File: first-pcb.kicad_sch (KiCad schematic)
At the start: 7 parts

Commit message: Schematic Complete
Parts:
- added K1: my_connector, Connector_PinHeader_2.54mm:PinHeader_1x02_P2.54mm_Vertical, symbol my_library:my_connector
- added unit 2 of U1
- added unit 3 of U1
- BT1: renamed from BT?; footprint (none) -> Battery:BatteryHolder_Eagle_12BH611-GR
- C1: renamed from C?; footprint (none) -> Capacitor_THT:C_Disc_D3.0mm_W2.0mm_P2.50mm
- P1: renamed from P?; footprint (none) -> Potentiometer_THT:Potentiometer_Alps_RK09K_Single_Vertical
- U1: renamed from U?; footprint (none) -> Package_DIP:DIP-8_W7.62mm
- gave numbers to parts that had none: 3
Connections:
- net GND: now also K1.2, U1.4 (V-)
- net at BT1.1 (+), Q1.1 (C), R1.1: now also U1.8 (V+)
- net at U1.1: now also Q1.2 (B)
- net at Q1.3 (E), U1.2 (-): now also K1.1
- no-connect marks 0 -> 3

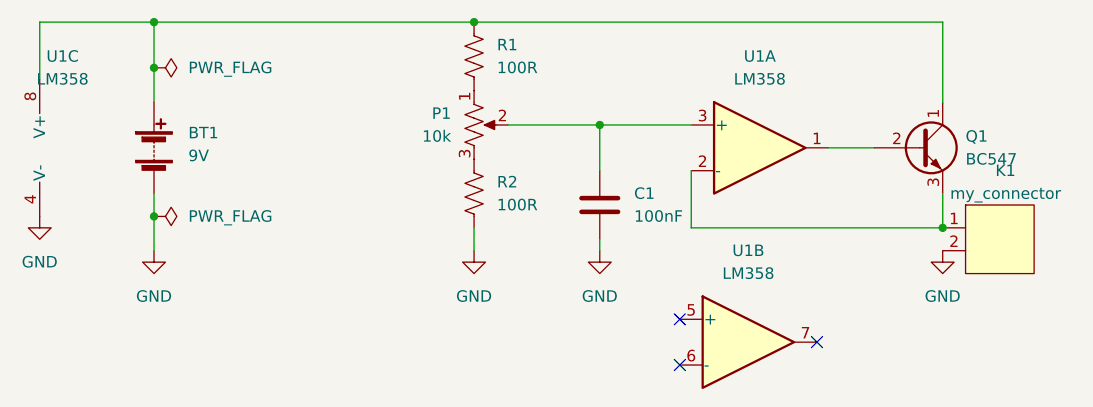
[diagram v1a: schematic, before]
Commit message: Add Grounding Pins/Mounting Holes
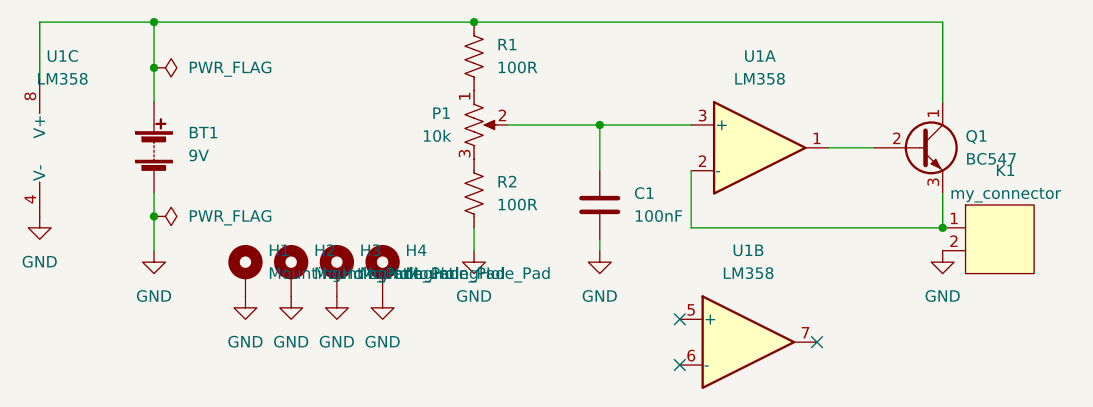
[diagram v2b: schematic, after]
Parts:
- added H1, H2, H3, H4: MountingHole_Pad, MountingHole:MountingHole_3.2mm_M3, symbol Mechanical:MountingHole_Pad
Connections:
- net GND: now also H1.1, H2.1, H3.1, H4.1
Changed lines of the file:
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@@
     (pin "2")
+  )
+  (symbol (lib_id "Mechanical:MountingHole_Pad") (at 67.31 106.68 0) (unit 1)
+    (in_bom yes) (on_board yes) (fields_autoplaced)
+    (property "Reference" "H4" (id 0) (at 69.85 104.1399 0)
+      (effects (font (size 1.27 1.27)) (justify left))
+    )
+    (property "Value" "MountingHole_Pad" (id 1) (at 69.85 106.6799 0)
+      (effects (font (size 1.27 1.27)) (justify left))
+    )
+    (property "Footprint" "MountingHole:MountingHole_3.2mm_M3" (id 2) (at 67.31 106.68 0)
+      (effects (font (size 1.27 1.27)) hide)
+    )
+    (property "Datasheet" "~" (id 3) (at 67.31 106.68 0)
+      (effects (font (size 1.27 1.27)) hide)
+    )
+    (pin "1")
+  )
+  (symbol (lib_id "power:GND") (at 52.07 109.22 0) (unit 1)
+    (in_bom yes) (on_board yes) (fields_autoplaced)
+    (property "Reference" "#PWR05" (id 0) (at 52.07 115.57 0)
+      (effects (font (size 1.27 1.27)) hide)
+    )
+    (property "Value" "GND" (id 1) (at 52.07 114.3 0))
+    (property "Footprint" "" (id 2) (at 52.07 109.22 0)
+      (effects (font (size 1.27 1.27)) hide)
+    )
+    (property "Datasheet" "" (id 3) (at 52.07 109.22 0)
+      (effects (font (size 1.27 1.27)) hide)
+    )
+    (pin "1")
   )
   (symbol (lib_id "Amplifier_Operational:LM358") (at 107.95 114.3 0) (unit 2)
@@
     (pin "1")
   )
+  (symbol (lib_id "power:GND") (at 57.15 109.22 0) (unit 1)
+    (in_bom yes) (on_board yes) (fields_autoplaced)
+    (property "Reference" "#PWR06" (id 0) (at 57.15 115.57 0)
+      (effects (font (size 1.27 1.27)) hide)
+    )
+    (property "Value" "GND" (id 1) (at 57.15 114.3 0))
+    (property "Footprint" "" (id 2) (at 57.15 109.22 0)
+      (effects (font (size 1.27 1.27)) hide)
+    )
+    (property "Datasheet" "" (id 3) (at 57.15 109.22 0)
+      (effects (font (size 1.27 1.27)) hide)
+    )
+    (pin "1")
+  )
+  (symbol (lib_id "Mechanical:MountingHole_Pad") (at 62.23 106.68 0) (unit 1)
+    (in_bom yes) (on_board yes) (fields_autoplaced)
+    (property "Reference" "H3" (id 0) (at 64.77 104.1399 0)
+      (effects (font (size 1.27 1.27)) (justify left))
+    )
+    (property "Value" "MountingHole_Pad" (id 1) (at 64.77 106.6799 0)
+      (effects (font (size 1.27 1.27)) (justify left))
+    )
+    (property "Footprint" "MountingHole:MountingHole_3.2mm_M3" (id 2) (at 62.23 106.68 0)
+      (effects (font (size 1.27 1.27)) hide)
+    )
+    (property "Datasheet" "~" (id 3) (at 62.23 106.68 0)
+      (effects (font (size 1.27 1.27)) hide)
+    )
+    (pin "1")
+  )
+  (symbol (lib_id "power:GND") (at 67.31 109.22 0) (unit 1)
+    (in_bom yes) (on_board yes) (fields_autoplaced)
+    (property "Reference" "#PWR08" (id 0) (at 67.31 115.57 0)
+      (effects (font (size 1.27 1.27)) hide)
+    )
+    (property "Value" "GND" (id 1) (at 67.31 114.3 0))
+    (property "Footprint" "" (id 2) (at 67.31 109.22 0)
+      (effects (font (size 1.27 1.27)) hide)
+    )
+    (property "Datasheet" "" (id 3) (at 67.31 109.22 0)
+      (effects (font (size 1.27 1.27)) hide)
+    )
+    (pin "1")
+  )
   (symbol (lib_id "power:GND") (at 129.54 104.14 0) (unit 1)
     (in_bom yes) (on_board yes) (fields_autoplaced)
@@
     (pin "1")
   )
+  (symbol (lib_id "power:GND") (at 62.23 109.22 0) (unit 1)
+    (in_bom yes) (on_board yes) (fields_autoplaced)
+    (property "Reference" "#PWR07" (id 0) (at 62.23 115.57 0)
+      (effects (font (size 1.27 1.27)) hide)
+    )
+    (property "Value" "GND" (id 1) (at 62.23 114.3 0))
+    (property "Footprint" "" (id 2) (at 62.23 109.22 0)
+      (effects (font (size 1.27 1.27)) hide)
+    )
+    (property "Datasheet" "" (id 3) (at 62.23 109.22 0)
+      (effects (font (size 1.27 1.27)) hide)
+    )
+    (pin "1")
+  )
   (symbol (lib_id "Device:R_US") (at 77.47 82.55 0) (unit 1)
     (in_bom yes) (on_board yes) (fields_autoplaced)
@@
     )
     (property "Datasheet" "~" (id 3) (at 41.91 100.33 0)
+      (effects (font (size 1.27 1.27)) hide)
+    )
+    (pin "1")
+  )
+  (symbol (lib_id "Mechanical:MountingHole_Pad") (at 57.15 106.68 0) (unit 1)
+    (in_bom yes) (on_board yes) (fields_autoplaced)
+    (property "Reference" "H2" (id 0) (at 59.69 104.1399 0)
+      (effects (font (size 1.27 1.27)) (justify left))
+    )
+    (property "Value" "MountingHole_Pad" (id 1) (at 59.69 106.6799 0)
+      (effects (font (size 1.27 1.27)) (justify left))
+    )
+    (property "Footprint" "MountingHole:MountingHole_3.2mm_M3" (id 2) (at 57.15 106.68 0)
+      (effects (font (size 1.27 1.27)) hide)
+    )
+    (property "Datasheet" "~" (id 3) (at 57.15 106.68 0)
       (effects (font (size 1.27 1.27)) hide)
     )
@@
     (pin "8")
   )
+  (symbol (lib_id "Mechanical:MountingHole_Pad") (at 52.07 106.68 0) (unit 1)
+    (in_bom yes) (on_board yes) (fields_autoplaced)
+    (property "Reference" "H1" (id 0) (at 54.61 104.1399 0)
+      (effects (font (size 1.27 1.27)) (justify left))
+    )
+    (property "Value" "MountingHole_Pad" (id 1) (at 54.61 106.6799 0)
+      (effects (font (size 1.27 1.27)) (justify left))
+    )
+    (property "Footprint" "MountingHole:MountingHole_3.2mm_M3" (id 2) (at 52.07 106.68 0)
+      (effects (font (size 1.27 1.27)) hide)
+    )
+    (property "Datasheet" "~" (id 3) (at 52.07 106.68 0)
+      (effects (font (size 1.27 1.27)) hide)
+    )
+    (pin "1")
+  )
   (symbol (lib_id "Device:R_US") (at 77.47 97.79 0) (unit 1)
     (in_bom yes) (on_board yes) (fields_autoplaced)
@@
       (reference "#PWR04") (unit 1) (value "GND") (footprint "")
     )
+    (path "/29a4dbbb-76df-4a5f-97bc-20e25b6c120d"
+      (reference "#PWR05") (unit 1) (value "GND") (footprint "")
+    )
+    (path "/6c5ddf50-598b-4624-97bc-707751a7cca0"
+      (reference "#PWR06") (unit 1) (value "GND") (footprint "")
+    )
+    (path "/ae2ab66b-9b4c-4dfe-8858-9502fff38c7b"
+      (reference "#PWR07") (unit 1) (value "GND") (footprint "")
+    )
+    (path "/939ef534-f1b7-45ad-a510-ae95db7deb2d"
+      (reference "#PWR08") (unit 1) (value "GND") (footprint "")
+    )
     (path "/64ebe1aa-d6a0-44a4-ab37-9850a83d8c0a"
       (reference "#PWR0101") (unit 1) (value "GND") (footprint "")
@@
       (reference "C1") (unit 1) (value "100nF") (footprint "Capacitor_THT:C_Disc_D3.0mm_W2.0mm_P2.50mm")
     )
+    (path "/e0ef2c2b-7a91-4865-8b62-e21cbba98aaa"
+      (reference "H1") (unit 1) (value "MountingHole_Pad") (footprint "MountingHole:MountingHole_3.2mm_M3")
+    )
+    (path "/d0603c93-1e0d-4f9c-9ae4-7cbc129674aa"
+      (reference "H2") (unit 1) (value "MountingHole_Pad") (footprint "MountingHole:MountingHole_3.2mm_M3")
+    )
+    (path "/85f2e531-45c2-4e3d-a8cf-17b5a7905d98"
+      (reference "H3") (unit 1) (value "MountingHole_Pad") (footprint "MountingHole:MountingHole_3.2mm_M3")
+    )
+    (path "/229409d0-9935-4be1-a852-23c013d0a939"
+      (reference "H4") (unit 1) (value "MountingHole_Pad") (footprint "MountingHole:MountingHole_3.2mm_M3")
+    )
     (path "/f45d5ac8-c98a-440b-a210-d962aa35e8d7"
